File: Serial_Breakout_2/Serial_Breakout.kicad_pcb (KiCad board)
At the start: 2 copper layers, 56.4 x 23.8 mm, 3 parts, among them J1 VIC Serial In, J2 Disc Serial Out, J3 Breakout

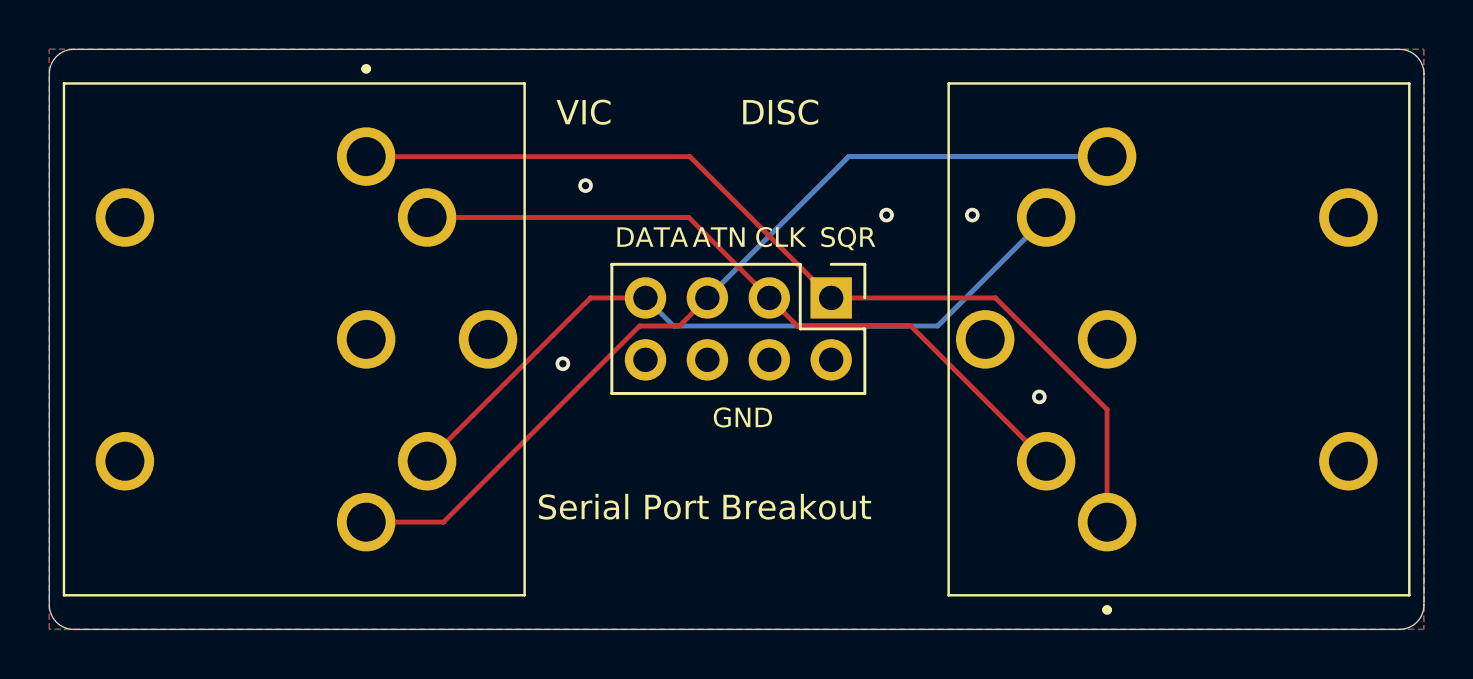
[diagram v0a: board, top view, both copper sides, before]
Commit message: Corrected pinout
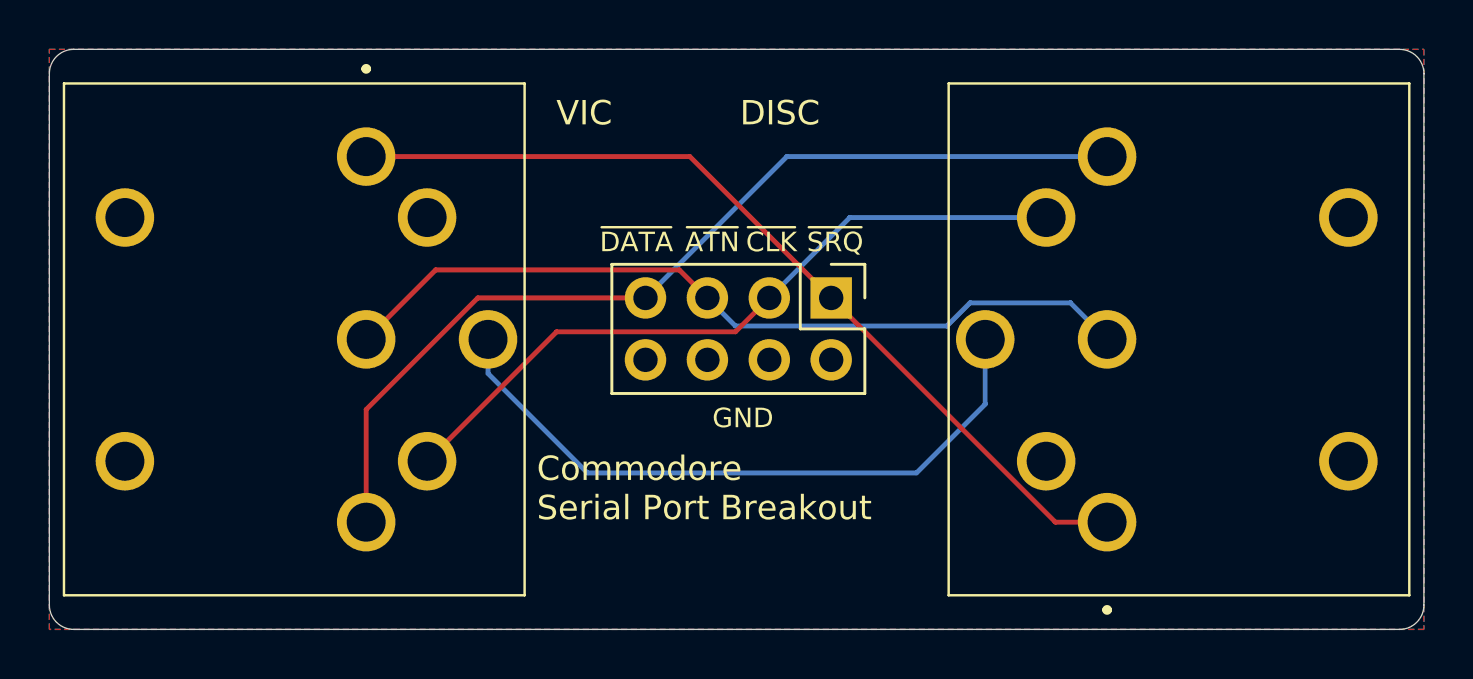
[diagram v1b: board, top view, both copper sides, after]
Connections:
- net /SERIAL ATN I/O renamed /~{ATN}
- net /SERIAL CLK I/O renamed /~{CLK}
- net /SERIAL DATA I/O renamed /~{DATA}
- net /SERIAL SRQ IN renamed /~{SRQIN}
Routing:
- net /~{RESET}: track 0.00 -> 27.3 mm
- net /~{DATA}: track 30.5 -> 39.3 mm
- net /~{ATN}: track 36.6 -> 33.6 mm
- net /~{SRQIN}: track 39.3 -> 36.6 mm
- net /GND: vias 5 -> 0
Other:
- board text added: "Commodore Serial Port Breakout"
- board text added: "~{ATN}"
- board text added: "~{CLK}"
- board text added: "~{DATA}"
- board text added: "~{SRQ}"
- board text removed: "ATN"
- board text removed: "CLK"
- board text removed: "DATA"
- board text removed: "SQR"
- board text removed: "Serial Port Breakout"
